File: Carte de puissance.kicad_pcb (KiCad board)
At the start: 4 copper layers, 73 x 98 mm, 96 parts, among them J1 5v external regulator, J2 other external regulator, J3 Pi_pwr, J4 Pi_data, J5 BAU1, J6 BAU2, J7 BAU3, J8 BAU4, J9 Programming, Q1 GSFP6901, Q2 GSFP6901, Q3 BC847, Q4 BC847, Q6 BC847, Q7 GSFP6901, Q8 BC847, SW1 SW_Push, SW2 Emergency switch (NC), U1 WeAct TPS5450 buck stepdown (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, U10 DPC817-B, U11 DPC817-B, U12 DPC817-B, U13 ATtiny1626-X, U2 WeAct TPS5450 buck stepdown (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, U3 WeAct TPS5450 buck stepdown (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, U5 PAC1811, U6 H11L1, U7 DPC817-B, U8 DPC817-B, U9 DPC817-B

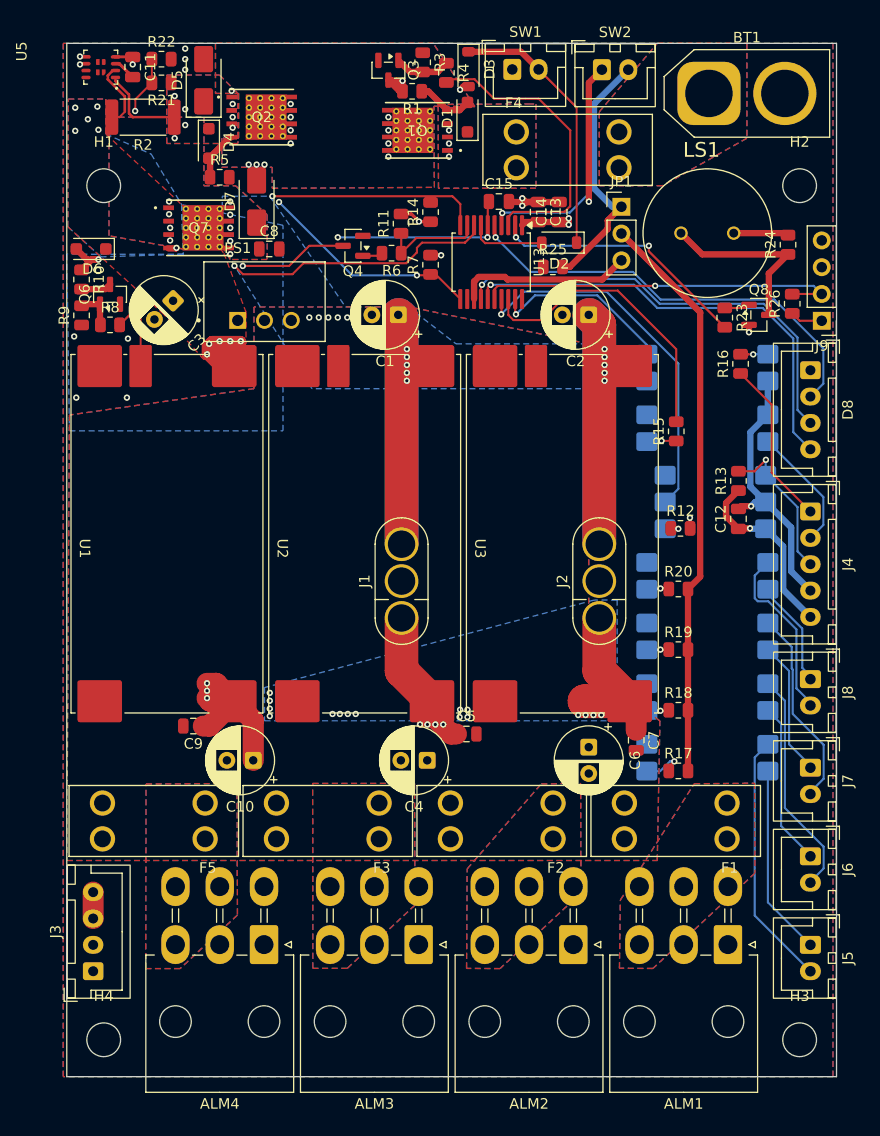
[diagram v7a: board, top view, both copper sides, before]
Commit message: Routing and debugging done, missing silkscreen
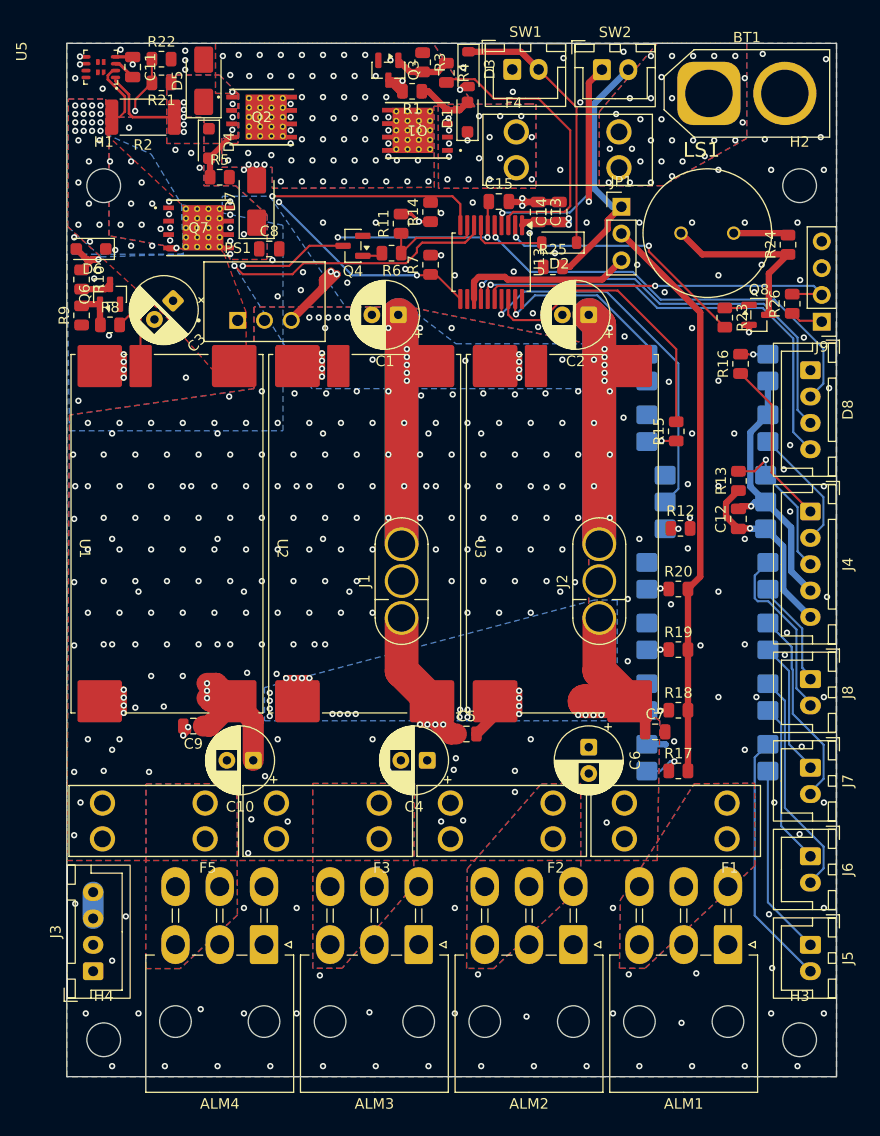
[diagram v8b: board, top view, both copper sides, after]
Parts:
- moved C7 1.97 mm to (140.5, 103.6), turned to 0 degrees
- moved J9 0.09 mm to (156.3, 64.7)
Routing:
- net GND: track 10.5 -> 64.0 mm, vias 13 -> 183
- net +V_5v: track 92.6 -> 107.3 mm
- net +VSW: track 16.3 -> 6.48 mm, vias 14 -> 39
- net VCC: track 58.5 -> 66.6 mm, vias 7 -> 9
- net +V_other: track 99.1 -> 96.3 mm
- net +V_PI: track 43.0 -> 43.7 mm
- net VSENSE+: vias 8 -> 9
- net Net-(Q1-Pad5): vias 8 -> 55
- net Net-(D1-K): vias 3 -> 16
- net +V_BATT: vias 21 -> 203
- net +BATT: vias 0 -> 29
